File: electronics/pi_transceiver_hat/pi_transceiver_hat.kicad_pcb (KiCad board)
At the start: 4 copper layers, 65 x 56 mm, 5 parts, among them J1 Raspberry_Pi_2_3

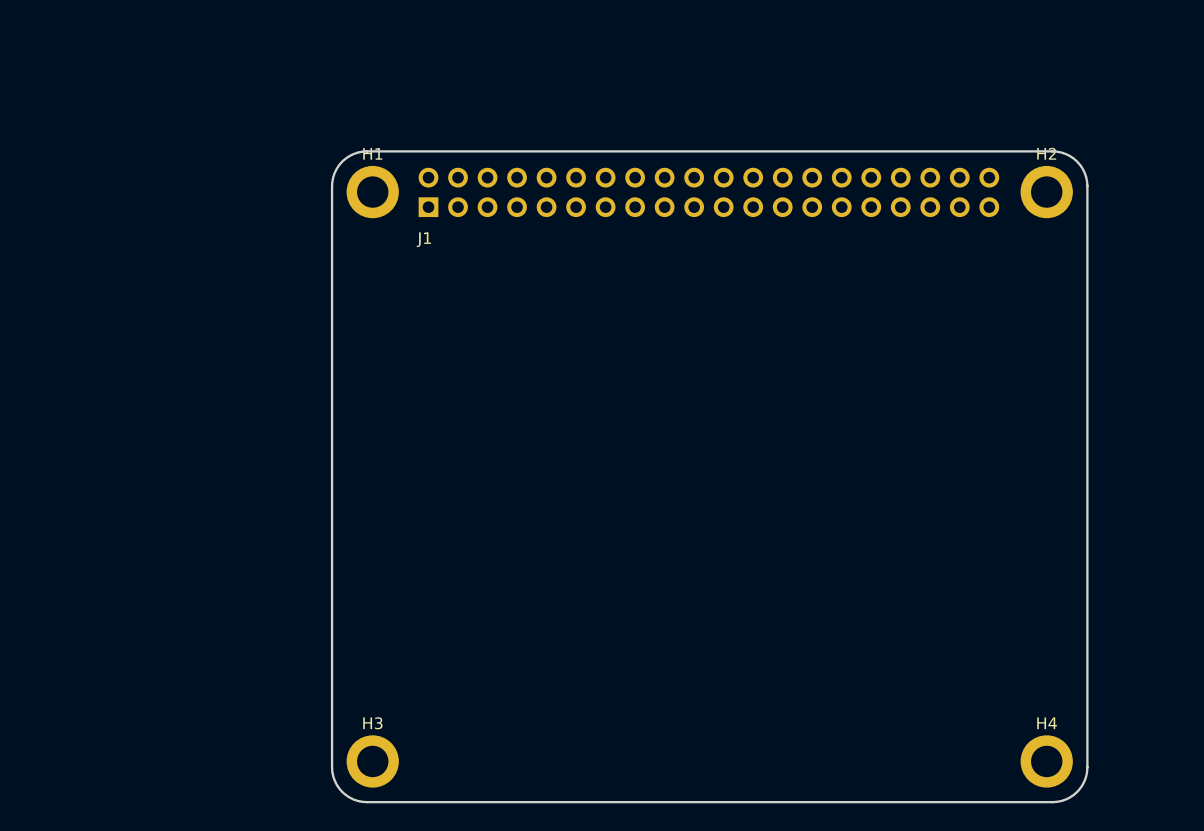
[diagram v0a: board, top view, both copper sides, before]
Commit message: More PCB hat design
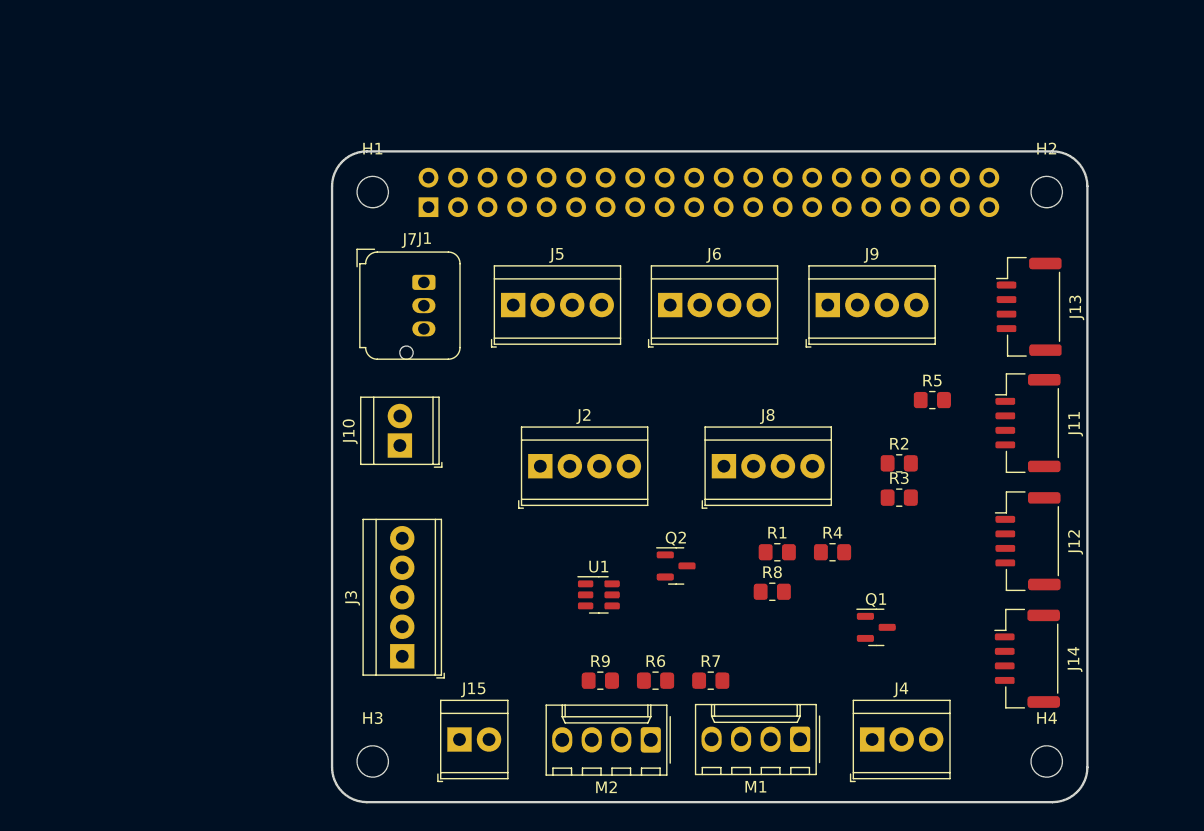
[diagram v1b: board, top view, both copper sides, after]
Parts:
- added J10: +5v Power, TerminalBlock_TE-Connectivity:TerminalBlock_TE_282834-2_1x02_P2.54mm_Horizontal, F.Cu at (110.3, 96.1)
- added J11: i2c, Connector_JST:JST_GH_BM04B-GHS-TBT_1x04-1MP_P1.25mm_Vertical, F.Cu at (164.4, 94.1)
- added J12: i2c, Connector_JST:JST_GH_BM04B-GHS-TBT_1x04-1MP_P1.25mm_Vertical, F.Cu at (164.4, 104.3)
- added J13: i2c, Connector_JST:JST_GH_BM04B-GHS-TBT_1x04-1MP_P1.25mm_Vertical, F.Cu at (164.5, 84.1)
- added J14: i2c, Connector_JST:JST_GH_BM04B-GHS-TBT_1x04-1MP_P1.25mm_Vertical, F.Cu at (164.3, 114.4)
- added J15: Meter, TerminalBlock_TE-Connectivity:TerminalBlock_TE_282834-2_1x02_P2.54mm_Horizontal, F.Cu at (115.5, 121.4)
- added J2: GND, TerminalBlock_TE-Connectivity:TerminalBlock_TE_282834-4_1x04_P2.54mm_Horizontal, F.Cu at (122.4, 97.8)
- added J3: RX Board, TerminalBlock_TE-Connectivity:TerminalBlock_TE_282834-5_1x05_P2.54mm_Horizontal, F.Cu at (110.5, 114.2)
- added J4: 1 wire, TerminalBlock_TE-Connectivity:TerminalBlock_TE_282834-3_1x03_P2.54mm_Horizontal, F.Cu at (151.0, 121.4)
- added J5: PSU Board, TerminalBlock_TE-Connectivity:TerminalBlock_TE_282834-4_1x04_P2.54mm_Horizontal, F.Cu at (120.1, 84.0)
- added J6: +5V, TerminalBlock_TE-Connectivity:TerminalBlock_TE_282834-4_1x04_P2.54mm_Horizontal, F.Cu at (133.6, 84.0)
- added J7: UART, Connector_JST:JST_JWPF_B03B-JWPF-SK-R_1x03_P2.00mm_Vertical, F.Cu at (112.4, 82.0)
- added J8: +3.3V, TerminalBlock_TE-Connectivity:TerminalBlock_TE_282834-4_1x04_P2.54mm_Horizontal, F.Cu at (138.2, 97.8)
- added J9: PA Board, TerminalBlock_TE-Connectivity:TerminalBlock_TE_282834-4_1x04_P2.54mm_Horizontal, F.Cu at (147.2, 84.0)
- added M1: Fan 1, Connector_Molex:Molex_KK-254_AE-6410-04A_1x04_P2.54mm_Vertical, F.Cu at (144.8, 121.3)
- added M2: Fan 2, Connector_Molex:Molex_KK-254_AE-6410-04A_1x04_P2.54mm_Vertical, F.Cu at (131.9, 121.4)
- added Q1: 2N7000, Package_TO_SOT_SMD:SOT-23, F.Cu at (151.3, 111.7)
- added Q2: 2N7000, Package_TO_SOT_SMD:SOT-23, F.Cu at (134.1, 106.4)
- added R1: 4.7K, Resistor_SMD:R_0805_2012Metric_Pad1.20x1.40mm_HandSolder, F.Cu at (142.8, 105.2)
- added R2: R, Resistor_SMD:R_0805_2012Metric_Pad1.20x1.40mm_HandSolder, F.Cu at (153.3, 97.6)
- added R3: 10K, Resistor_SMD:R_0805_2012Metric_Pad1.20x1.40mm_HandSolder, F.Cu at (153.3, 100.5)
- added R4: R, Resistor_SMD:R_0805_2012Metric_Pad1.20x1.40mm_HandSolder, F.Cu at (147.6, 105.2)
- added R5: 10K, Resistor_SMD:R_0805_2012Metric_Pad1.20x1.40mm_HandSolder, F.Cu at (156.2, 92.2)
- added R6: 10K, Resistor_SMD:R_0805_2012Metric_Pad1.20x1.40mm_HandSolder, F.Cu at (132.3, 116.3)
- added R7: 10K, Resistor_SMD:R_0805_2012Metric_Pad1.20x1.40mm_HandSolder, F.Cu at (137.1, 116.3)
- added R8: 2K, Resistor_SMD:R_0805_2012Metric_Pad1.20x1.40mm_HandSolder, F.Cu at (142.4, 108.6)
- added R9: 2K, Resistor_SMD:R_0805_2012Metric_Pad1.20x1.40mm_HandSolder, F.Cu at (127.6, 116.3)
- added U1: MCP4725xxx-xCH, Package_TO_SOT_SMD:SOT-23-6, F.Cu at (127.5, 108.9)
- H1, H2, H3, H4: value MountingHole -> MountingHole_Pad; footprint MountingHole:MountingHole_2.7mm_M2.5_ISO14580_Pad -> MountingHole:MountingHole_2.7mm_M2.5
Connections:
- J1 pad 1: unconnected-(J1-Pad1) -> +3V3
- J1 pad 10: unconnected-(J1-Pad10) -> Net-(J1-Pad10)
- J1 pad 11: unconnected-(J1-Pad11) -> Net-(J1-Pad11)
- J1 pad 12: unconnected-(J1-Pad12) -> Net-(J1-Pad12)
- J1 pad 13: unconnected-(J1-Pad13) -> Net-(J1-Pad13)
- J1 pad 14: unconnected-(J1-Pad14) -> GND
- J1 pad 15: unconnected-(J1-Pad15) -> Net-(J1-Pad15)
- J1 pad 16: unconnected-(J1-Pad16) -> Net-(J1-Pad16)
- J1 pad 17: unconnected-(J1-Pad17) -> +3V3
- J1 pad 2: unconnected-(J1-Pad2) -> +5V
- J1 pad 20: unconnected-(J1-Pad20) -> GND
- J1 pad 25: unconnected-(J1-Pad25) -> GND
- J1 pad 29: unconnected-(J1-Pad29) -> Net-(J1-Pad29)
- J1 pad 3: unconnected-(J1-Pad3) -> Net-(J1-Pad3)
- J1 pad 30: unconnected-(J1-Pad30) -> GND
- J1 pad 31: unconnected-(J1-Pad31) -> Net-(J1-Pad31)
- J1 pad 32: unconnected-(J1-Pad32) -> Net-(J1-Pad32)
- J1 pad 33: unconnected-(J1-Pad33) -> Net-(J1-Pad33)
- J1 pad 34: unconnected-(J1-Pad34) -> GND
- J1 pad 36: unconnected-(J1-Pad36) -> Net-(J1-Pad36)
- J1 pad 37: unconnected-(J1-Pad37) -> Net-(J1-Pad37)
- J1 pad 38: unconnected-(J1-Pad38) -> Net-(J1-Pad38)
- J1 pad 39: unconnected-(J1-Pad39) -> GND
- J1 pad 4: unconnected-(J1-Pad4) -> +5V
- J1 pad 40: unconnected-(J1-Pad40) -> Net-(J1-Pad40)
- J1 pad 5: unconnected-(J1-Pad5) -> Net-(J1-Pad5)
- J1 pad 6: unconnected-(J1-Pad6) -> GND
- J1 pad 8: unconnected-(J1-Pad8) -> Net-(J1-Pad8)
- J1 pad 9: unconnected-(J1-Pad9) -> GND
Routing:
- added copper zone on In1.Cu, net GND
- added copper zone on In2.Cu, net Net-(J1-Pad29)
- removed copper zone on In2.Cu, net unconnected-(J1-Pad29)
- removed copper zone on In1.Cu, net unconnected-(J1-Pad6)

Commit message: More PCB updates
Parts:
- moved J4 48.4 mm to (121.3, 83.1)
- moved J5 47.8 mm to (150.0, 121.3)
- moved M2 45.2 mm to (156.0, 83.1)
- moved M1 38.3 mm to (142.6, 83.1)
- moved J9 32.1 mm to (123.9, 106.1)
- moved R9 30.8 mm to (146.1, 91.6), turned to 90 degrees
- moved R7 28.5 mm to (148.9, 90.3), turned to -90 degrees
- moved R1 24.1 mm to (125.1, 89.0)
- moved J2 23.6 mm to (123.6, 121.4)
- moved J8 23.5 mm to (137.2, 121.4)
- moved J6 23.5 mm to (141.4, 106.1)
- moved R6 23.0 mm to (134.7, 93.4), turned to -90 degrees
- moved Q1 22.9 mm to (154.2, 89.0)
- moved R8 20.7 mm to (134.9, 89.4)
- moved Q2 18.8 mm to (142.0, 89.4)
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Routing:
- net Net-(J1-Pad40): track 0.00 -> 49.7 mm
- net Net-(J1-Pad38): track 0.00 -> 49.7 mm
- net Net-(J1-Pad36): track 0.00 -> 49.7 mm
- net Net-(J15-Pad2): track 0.00 -> 10.7 mm
- net Net-(J1-Pad3): track 0.00 -> 10.3 mm
- net Net-(J1-Pad5): track 0.00 -> 9.53 mm
- added copper zone on In2.Cu, net +5V
- removed copper zone on In2.Cu, net Net-(J1-Pad29)

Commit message: More hat board design.
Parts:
- removed R2, R4: R, Resistor_SMD:R_0805_2012Metric_Pad1.20x1.40mm_HandSolder
- moved R3 16.5 mm to (135.2, 93.3), turned to 90 degrees
- moved Q1 15.1 mm to (139.8, 93.2)
- moved Q2 11.5 mm to (152.9, 93.2)
- moved R6 9.53 mm to (143.3, 89.2), turned to 180 degrees
- moved R5 8.55 mm to (148.4, 93.3), turned to 90 degrees
- moved R7 6.45 mm to (155.2, 89.2), turned to 180 degrees
- moved R9 4.15 mm to (149.4, 89.2), turned to 180 degrees
- moved R8 1.13 mm to (136.0, 89.2), turned to 180 degrees
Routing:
- net +3V3: track 0.00 -> 192.3 mm, vias 0 -> 5
- net Net-(J1-Pad3): track 10.3 -> 178.8 mm
- net Net-(J1-Pad5): track 9.53 -> 126.8 mm
- net Net-(J1-Pad37): track 0.00 -> 60.0 mm
- net Net-(J1-Pad12): track 0.00 -> 51.0 mm
- net Net-(J1-Pad11): track 0.00 -> 39.7 mm
- net Net-(J1-Pad13): track 0.00 -> 39.0 mm
- net Net-(J1-Pad16): track 0.00 -> 36.8 mm
- net Net-(J1-Pad15): track 0.00 -> 35.2 mm
- net Net-(J1-Pad32): track 0.00 -> 31.1 mm
- net Net-(J1-Pad33): track 0.00 -> 27.3 mm
- net GND: track 0.00 -> 19.6 mm, vias 0 -> 7
- net Net-(J1-Pad10): track 0.00 -> 17.4 mm
- net +5V: track 0.00 -> 14.9 mm, vias 0 -> 1
- net Net-(J1-Pad8): track 0.00 -> 14.3 mm
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- added copper zone on F.Cu, net GND

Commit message: PCB updates for hat.
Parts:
- added C1: 10uF, Capacitor_SMD:CP_Elec_10x12.6, F.Cu at (84.7, 89.3)
- added C2: 100nF, Capacitor_SMD:C_0805_2012Metric_Pad1.18x1.45mm_HandSolder, F.Cu at (94.5, 87.9)
- added C3: C, Capacitor_SMD:C_0805_2012Metric_Pad1.18x1.45mm_HandSolder, F.Cu at (84.6, 96.7)
- added C4: C, Capacitor_SMD:C_0805_2012Metric_Pad1.18x1.45mm_HandSolder, F.Cu at (79.8, 96.7)
- added C5: C, Capacitor_SMD:C_0805_2012Metric_Pad1.18x1.45mm_HandSolder, F.Cu at (94.5, 84.9)
- added R10: 4.7K, Resistor_SMD:R_0805_2012Metric_Pad1.20x1.40mm_HandSolder, F.Cu at (89.4, 96.7)
- added R11: 0R, Resistor_SMD:R_0805_2012Metric_Pad1.20x1.40mm_HandSolder, F.Cu at (99.2, 84.9)
- added R2: 4.7K, Resistor_SMD:R_0805_2012Metric_Pad1.20x1.40mm_HandSolder, F.Cu at (94.4, 90.9)
- added R4: 4.7K, Resistor_SMD:R_0805_2012Metric_Pad1.20x1.40mm_HandSolder, F.Cu at (99.2, 87.8)
- J11, J12, J13, J14: footprint Connector_JST:JST_GH_BM04B-GHS-TBT_1x04-1MP_P1.25mm_Vertical -> Connector_JST:JST_XH_B4B-XH-A_1x04_P2.50mm_Vertical
- J7: footprint Connector_JST:JST_JWPF_B03B-JWPF-SK-R_1x03_P2.00mm_Vertical -> Connector_JST:JST_XH_B3B-XH-A_1x03_P2.50mm_Vertical
- moved J6 4.63 mm to (136.8, 106.0)
- moved J13 3.80 mm to (164.6, 80.3)
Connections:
- U1 pad 6: unconnected-(U1-Pad6) -> Net-(U1-Pad6)
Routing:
- net Net-(J1-Pad3): track 178.8 -> 0.00 mm
- net +3V3: track 192.3 -> 371.0 mm

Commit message: Hat PCB alpha design
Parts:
- C1: footprint Capacitor_SMD:CP_Elec_10x12.6 -> Capacitor_SMD:CP_Elec_4x5.4
- C3, C4, C5: value C -> 100nF
- moved C4 51.7 mm to (131.2, 102.7)
- moved C5 43.1 mm to (124.2, 116.1)
- moved C3 41.5 mm to (126.1, 96.0), turned to 180 degrees
- moved R10 40.1 mm to (126.6, 111.8), turned to 180 degrees
- moved R4 36.4 mm to (131.2, 105.2), turned to 180 degrees
- moved C1 35.3 mm to (119.3, 96.5)
- moved C2 34.6 mm to (129.1, 88.0)
- moved R11 34.3 mm to (122.5, 110.0), turned to 180 degrees
- moved R2 32.5 mm to (126.1, 98.3)
- moved J12 9.51 mm to (154.9, 103.6)
- moved J9 5.78 mm to (118.4, 104.3)
- moved J14 5.43 mm to (165.0, 109.0)
- moved R1 3.46 mm to (121.7, 89.5), turned to 180 degrees
- moved J7 2.45 mm to (110.2, 83.0)
- moved J6 1.65 mm to (136.5, 104.4)
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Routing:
- net +3V3: track 371.0 -> 197.8 mm, vias 5 -> 3
- net Net-(C4-Pad2): track 0.00 -> 161.6 mm
- net Net-(J1-Pad36): track 49.7 -> 62.4 mm
- net +5V: track 14.9 -> 26.7 mm, vias 1 -> 2
- net GND: track 19.6 -> 13.0 mm, vias 7 -> 11
- net Net-(C2-Pad1): track 60.0 -> 66.3 mm
- net Net-(R10-Pad2): track 0.00 -> 4.46 mm
- net Net-(J1-Pad10): track 17.4 -> 13.4 mm
- net Net-(J1-Pad12): track 51.0 -> 53.3 mm
- net Net-(J1-Pad8): track 14.3 -> 13.7 mm
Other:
- board text added: "RADARC pi-transceiver hat https://github.com/M0LTE/pi-transceiver"

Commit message: Gerber generation for hat.
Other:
- rule pad_to_mask_clearance: 0.051 -> 0
